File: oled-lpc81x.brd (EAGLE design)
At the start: 22.2 x 18.1 mm, 14 parts, among them X1 PIIKKIRIMA-2X8, X2 PIIKKIRIMA-8

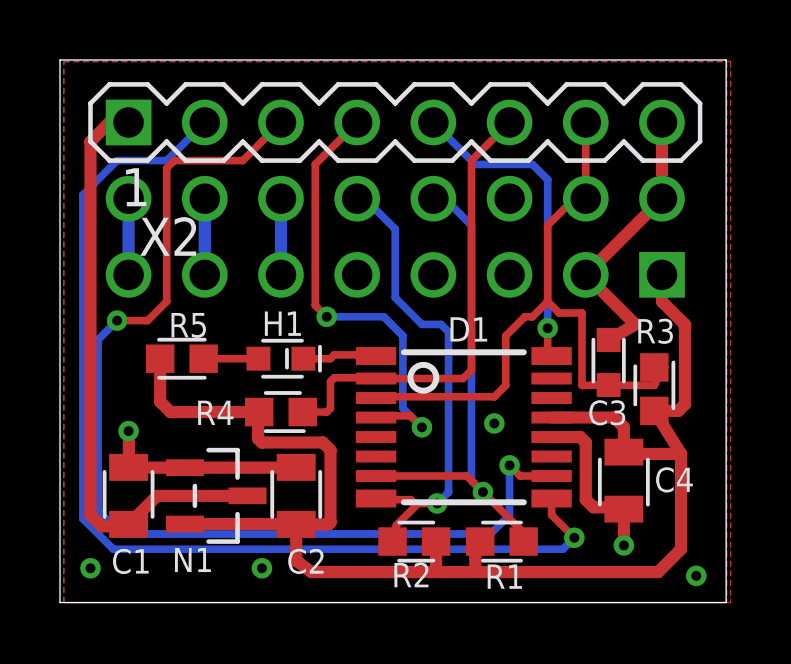
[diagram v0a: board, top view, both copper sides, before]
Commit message: Changed busses
OLED now 3-wire SPI
I2C external to header
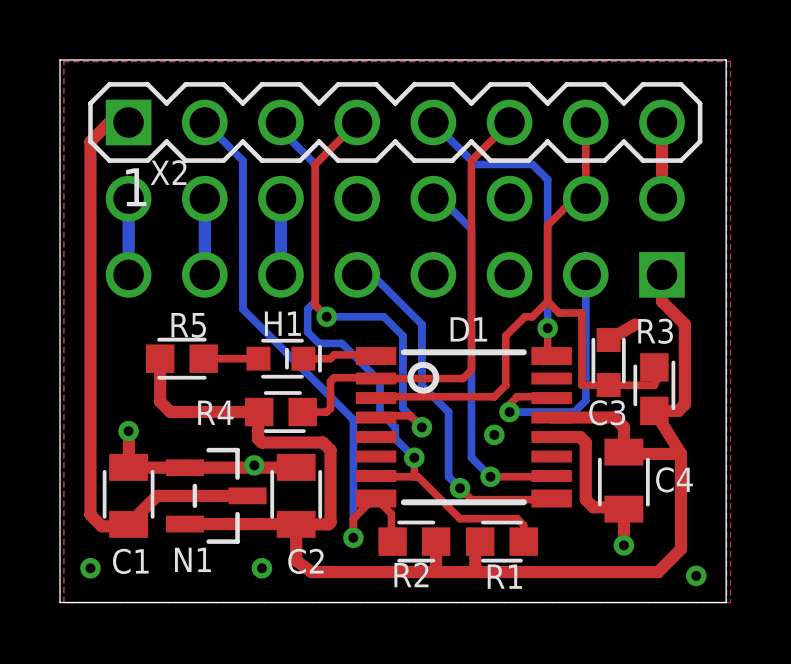
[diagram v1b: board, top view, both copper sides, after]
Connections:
- removed net PIO01: D1.9, X2.2
- removed net PIO09: D1.10, X2.3
- new net CSN: D1.14, X1.3
- new net SCLK: D1.10, X1.8
- new net SDATA: D1.9, X1.9
- net GND: no longer X1.3
- net SCL: now also X2.3; no longer X1.8
- net SDA: now also X2.2; no longer X1.10
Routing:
- net PIO09: track 34.9 -> 0.00 mm, vias 2 -> 0
- net PIO01: track 34.4 -> 0.00 mm, vias 1 -> 0
- net SCLK: track 0.00 -> 12.3 mm, vias 0 -> 1
- net SDATA: track 0.00 -> 12.1 mm, vias 0 -> 1
- net CSN: track 0.00 -> 8.67 mm, vias 0 -> 1
- net GND: track 29.8 -> 23.9 mm, vias 6 -> 7
- net SCL: track 16.7 -> 20.5 mm
- net SDA: track 15.8 -> 19.2 mm
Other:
- board text added: "SCL"
- board text added: "SDA"
- board text removed: "P01"
- board text removed: "P09"

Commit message: v2 - VDD/VSS connection to LPC812 corrected.
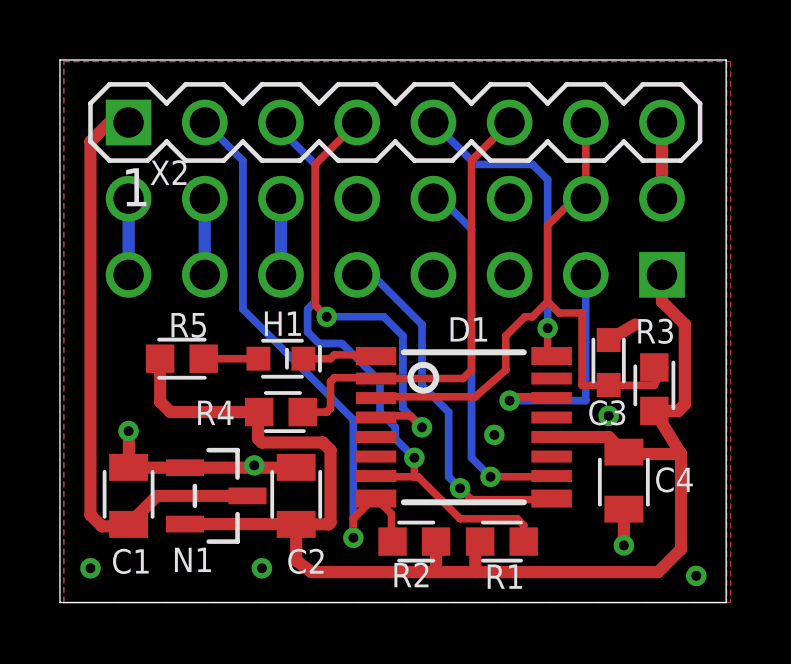
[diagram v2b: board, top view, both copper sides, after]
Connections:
- net +3V3: now also D1.12; no longer D1.13
- net GND: now also D1.13; no longer D1.12
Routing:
- net GND: track 23.9 -> 19.4 mm, vias 7 -> 8
- net +3V3: track 48.4 -> 47.6 mm
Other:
- board text added: "KL 2013 V2"
- board text removed: "KL 2013"
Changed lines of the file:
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@@
 <layer number="14" name="Route14" color="1" fill="6" visible="no" active="no"/>
 <layer number="15" name="Route15" color="4" fill="6" visible="no" active="no"/>
-<layer number="16" name="Bottom" color="6" fill="1" visible="yes" active="yes"/>
+<layer number="16" name="Bottom" color="6" fill="1" visible="no" active="yes"/>
 <layer number="17" name="Pads" color="2" fill="1" visible="yes" active="yes"/>
 <layer number="18" name="Vias" color="2" fill="1" visible="yes" active="yes"/>
-<layer number="19" name="Unrouted" color="6" fill="1" visible="no" active="yes"/>
+<layer number="19" name="Unrouted" color="6" fill="1" visible="yes" active="yes"/>
 <layer number="20" name="Dimension" color="15" fill="1" visible="no" active="yes"/>
-<layer number="21" name="tPlace" color="12" fill="1" visible="no" active="yes"/>
+<layer number="21" name="tPlace" color="12" fill="1" visible="yes" active="yes"/>
 <layer number="22" name="bPlace" color="9" fill="1" visible="yes" active="yes"/>
 <layer number="23" name="tOrigins" color="15" fill="1" visible="no" active="yes"/>
 <layer number="24" name="bOrigins" color="15" fill="1" visible="yes" active="yes"/>
-<layer number="25" name="tNames" color="12" fill="1" visible="no" active="yes"/>
-<layer number="26" name="bNames" color="9" fill="1" visible="yes" active="yes"/>
+<layer number="25" name="tNames" color="12" fill="1" visible="yes" active="yes"/>
+<layer number="26" name="bNames" color="9" fill="1" visible="no" active="yes"/>
 <layer number="27" name="tValues" color="7" fill="1" visible="no" active="yes"/>
 <layer number="28" name="bValues" color="7" fill="1" visible="no" active="yes"/>
@@
 <wire x1="41.509" y1="35.103" x2="19.304" y2="35.103" width="0" layer="20"/>
 <wire x1="19.304" y1="35.103" x2="19.304" y2="17.018" width="0" layer="20"/>
-<text x="38.481" y="23.622" size="1.524" layer="22" font="vector" rot="MR0">LPC81X-OLED</text>
-<text x="34.798" y="18.415" size="1.27" layer="22" font="vector" rot="MR0">KL 2013</text>
+<text x="37.846" y="24.13" size="1.524" layer="22" font="vector" rot="MR0">LPC81X-OLED</text>
+<text x="37.465" y="18.796" size="1.27" layer="22" font="vector" rot="MR0">KL 2013 V2</text>
 <wire x1="22.606" y1="25.781" x2="24.13" y2="25.781" width="0.127" layer="21"/>
 <wire x1="22.606" y1="24.511" x2="24.13" y2="24.511" width="0.127" layer="21"/>
@@
 <contactref element="C2" pad="1"/>
 <contactref element="N1" pad="2"/>
-<contactref element="D1" pad="13"/>
 <contactref element="R4" pad="2"/>
 <contactref element="R3" pad="2"/>
@@
 <wire x1="25.908" y1="23.331" x2="25.945" y2="23.368" width="0.4064" layer="1"/>
 <contactref element="C4" pad="1"/>
-<wire x1="35.691" y1="23.185" x2="37.775" y2="23.185" width="0.4064" layer="1"/>
-<wire x1="37.775" y1="23.185" x2="38.1" y2="22.86" width="0.4064" layer="1"/>
-<wire x1="38.1" y1="22.86" x2="38.1" y2="22.032" width="0.4064" layer="1"/>
 <wire x1="39.116" y1="23.405" x2="40.005" y2="21.971" width="0.4064" layer="1"/>
 <wire x1="40.005" y1="21.971" x2="38.161" y2="21.971" width="0.4064" layer="1"/>
@@
 <wire x1="40.132" y1="26.289" x2="39.37" y2="27.051" width="0.4064" layer="1"/>
 <wire x1="39.37" y1="27.051" x2="39.37" y2="27.94" width="0.4064" layer="1"/>
+<contactref element="D1" pad="12"/>
+<wire x1="35.691" y1="22.535" x2="37.597" y2="22.535" width="0.4064" layer="1"/>
+<wire x1="37.597" y1="22.535" x2="38.1" y2="22.032" width="0.4064" layer="1"/>
 </signal>
 <signal name="GND">
@@
 <contactref element="C1" pad="2"/>
 <contactref element="C2" pad="2"/>
-<contactref element="D1" pad="12"/>
 <contactref element="C3" pad="2"/>
 <contactref element="X2" pad="8"/>
@@
 <wire x1="27.1678" y1="21.5138" x2="27.178" y2="21.524" width="0.4064" layer="1"/>
 <contactref element="C4" pad="2"/>
-<wire x1="35.691" y1="22.535" x2="36.647" y2="22.535" width="0.4064" layer="1"/>
-<wire x1="36.647" y1="22.535" x2="36.83" y2="22.352" width="0.4064" layer="1"/>
-<wire x1="36.83" y1="22.352" x2="36.83" y2="20.447" width="0.4064" layer="1"/>
-<wire x1="36.83" y1="20.447" x2="37.084" y2="20.193" width="0.4064" layer="1"/>
-<wire x1="37.084" y1="20.193" x2="38.039" y2="20.193" width="0.4064" layer="1"/>
 <wire x1="38.039" y1="20.193" x2="38.1" y2="20.132" width="0.4064" layer="1"/>
 <wire x1="38.1" y1="20.132" x2="38.1" y2="18.923" width="0.4064" layer="1"/>
@@
 <via x="26.035" y="18.161" extent="1-16" drill="0.3302"/>
 <via x="25.781" y="21.59" extent="1-16" drill="0.3302"/>
-<wire x1="27.0866" y1="21.6154" x2="25.781" y2="21.59" width="0" layer="19" extent="1-1"/>
+<contactref element="D1" pad="13"/>
+<via x="37.592" y="23.241" extent="1-16" drill="0.3302"/>
 </signal>
 <signal name="RESETN">
@@
 <wire x1="35.052" y1="26.543" x2="34.798" y2="26.543" width="0.254" layer="1"/>
 <wire x1="34.798" y1="26.543" x2="34.163" y2="25.908" width="0.254" layer="1"/>
-<wire x1="34.163" y1="25.908" x2="34.163" y2="24.257" width="0.254" layer="1"/>
-<wire x1="34.163" y1="24.257" x2="33.782" y2="23.876" width="0.254" layer="1"/>
-<wire x1="33.782" y1="23.876" x2="29.882" y2="23.876" width="0.254" layer="1"/>
+<wire x1="34.163" y1="25.908" x2="34.163" y2="24.765" width="0.254" layer="1"/>
+<wire x1="34.163" y1="24.765" x2="33.147" y2="23.876" width="0.254" layer="1"/>
+<wire x1="33.147" y1="23.876" x2="29.882" y2="23.876" width="0.254" layer="1"/>
 <wire x1="29.882" y1="23.876" x2="29.841" y2="23.835" width="0.254" layer="1"/>
 <wire x1="39.116" y1="24.855" x2="39.46" y2="24.855" width="0.254" layer="1"/>
@@
 <contactref element="D1" pad="14"/>
 <wire x1="36.83" y1="27.94" x2="36.83" y2="23.749" width="0.254" layer="16"/>
-<wire x1="36.83" y1="23.749" x2="36.449" y2="23.368" width="0.254" layer="16"/>
-<wire x1="36.449" y1="23.368" x2="34.29" y2="23.368" width="0.254" layer="16"/>
-<via x="34.29" y="23.368" extent="1-16" drill="0.3302"/>
-<wire x1="34.29" y1="23.368" x2="34.29" y2="23.622" width="0.254" layer="1"/>
+<wire x1="36.83" y1="23.749" x2="34.29" y2="23.749" width="0.254" layer="16"/>
+<via x="34.29" y="23.749" extent="1-16" drill="0.3302"/>
+<wire x1="34.29" y1="23.749" x2="34.29" y2="23.622" width="0.254" layer="1"/>
 <wire x1="34.29" y1="23.622" x2="34.544" y2="23.876" width="0.254" layer="1"/>
 <wire x1="34.544" y1="23.876" x2="35.65" y2="23.876" width="0.254" layer="1"/>
